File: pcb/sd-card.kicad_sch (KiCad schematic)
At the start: 7 parts, among them J7 MicroSD_5033981892, U7 AP22615AWU-7

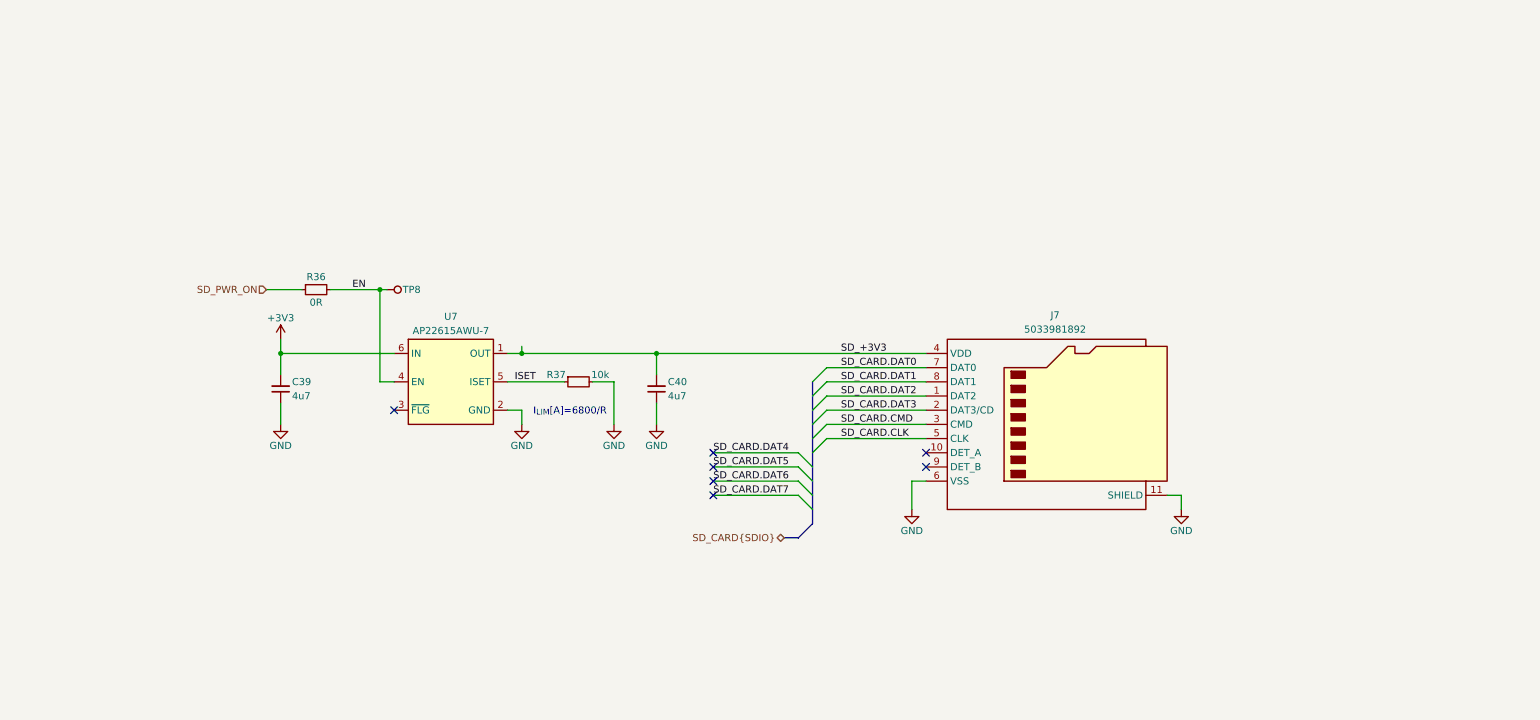
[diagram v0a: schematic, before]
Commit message: [#5] Refactor the schematic
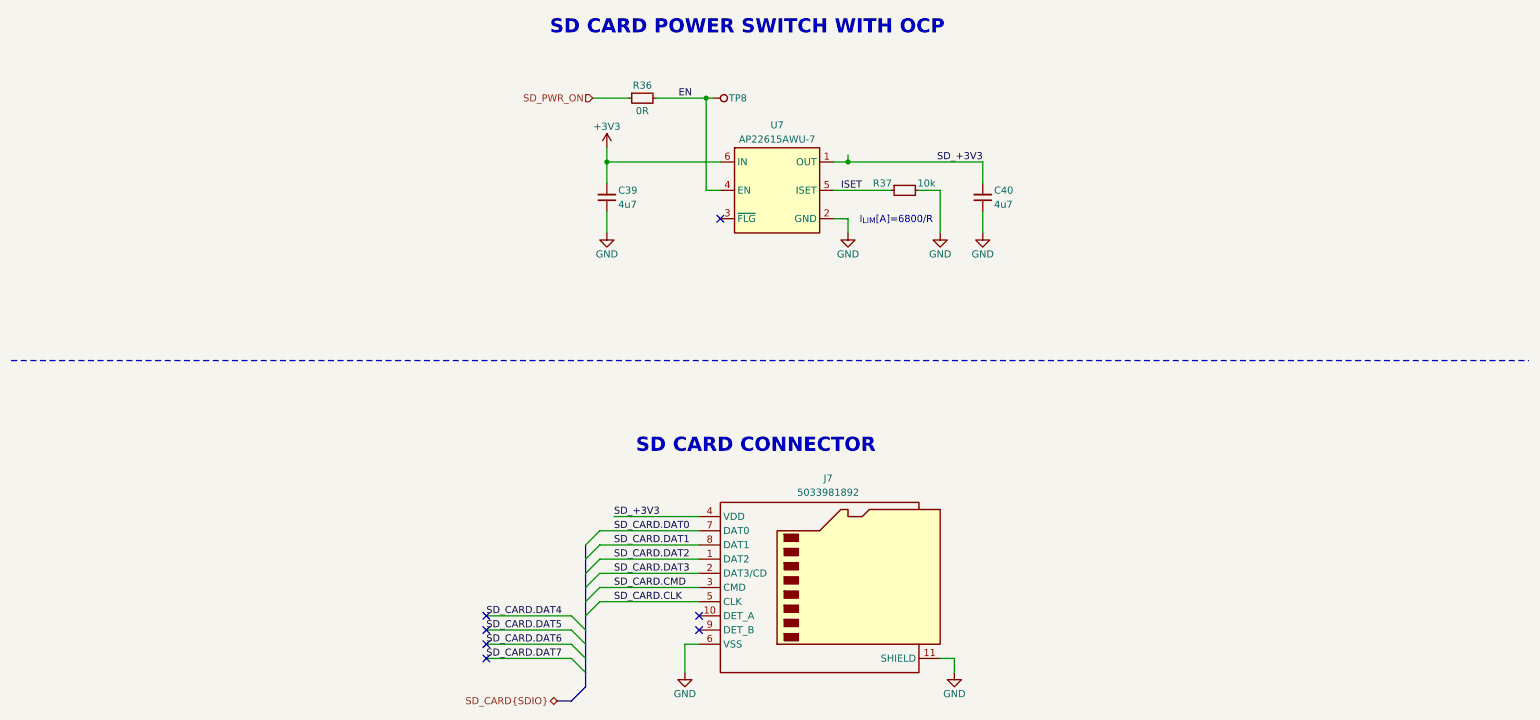
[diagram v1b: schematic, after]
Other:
- note added: "SD CARD CONNECTOR"
- note added: "SD CARD POWER SWITCH WITH OCP"
- moved on the sheet: C39, C40, J7, R36, R37, TP8, U7

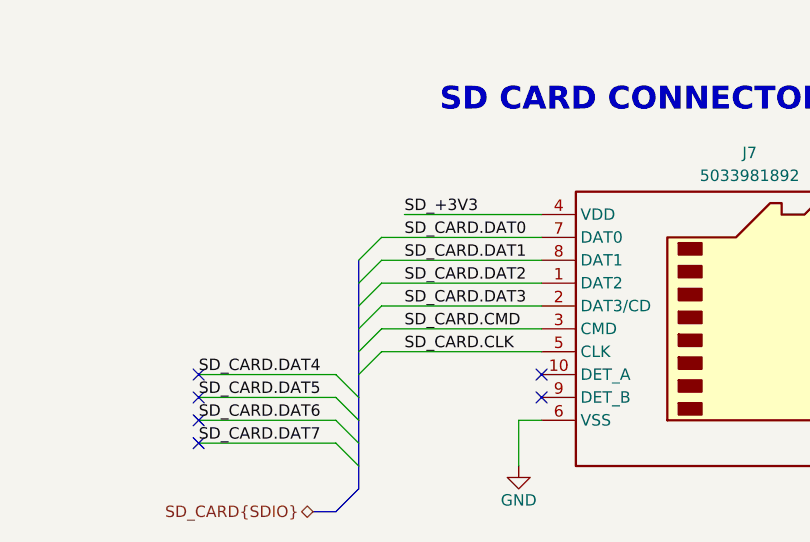
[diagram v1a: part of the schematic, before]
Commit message: [#5] Add decoupling capacitor closer to the SD card, update programming connector from library
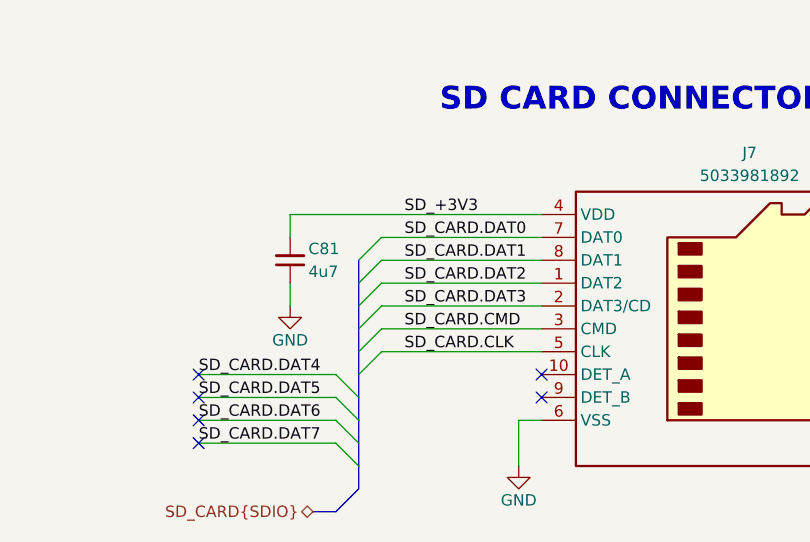
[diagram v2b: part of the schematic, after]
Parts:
- added C81: C-4u7-0402, DW-footprints:C_0402_1005Metric, symbol DW-capacitors:C-4u7-0402
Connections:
- net GND: now also C81.1
- net SD_+3V3: now also C81.2
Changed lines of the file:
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@@
+	(wire
+		(pts
+			(xy 107.95 129.54) (xy 107.95 127)
+		)
+		(stroke
+			(width 0)
+			(type default)
+		)
+	)
 	(wire
 		(pts
@@
 		)
 	)
+	(wire
+		(pts
+			(xy 107.95 127) (xy 135.89 127)
+		)
+		(stroke
+			(width 0)
+			(type default)
+		)
+	)
 	(bus
 		(pts
@@
 		)
 	)
+	(wire
+		(pts
+			(xy 107.95 134.62) (xy 107.95 137.16)
+		)
+		(stroke
+			(width 0)
+			(type default)
+		)
+	)
 	(bus
 		(pts
@@
 		(pts
 			(xy 186.69 72.39) (xy 186.69 76.2)
-		)
-		(stroke
-			(width 0)
-			(type default)
-		)
-	)
-	(wire
-		(pts
-			(xy 120.65 127) (xy 135.89 127)
 		)
 		(stroke
@@
 					(size 1.27 1.27)
 					(italic yes)
+				)
+			)
+		)
+	)
+	(symbol
+		(lib_id "DW-capacitors:C-4u7-0402")
+		(at 107.95 134.62 90)
+		(unit 1)
+		(exclude_from_sim no)
+		(in_bom yes)
+		(on_board yes)
+		(dnp no)
+		(property "Reference" "C81"
+			(at 109.982 130.81 90)
+			(effects
+				(font
+					(size 1.27 1.27)
+					(thickness 0.15)
+				)
+				(justify right)
+			)
+		)
+		(property "Value" "C-4u7-0402"
+			(at 110.49 121.92 0)
+			(effects
+				(font
+					(size 1.27 1.27)
+					(thickness 0.15)
+				)
+				(justify left bottom)
+				(hide yes)
+			)
+		)
+		(property "Footprint" "DW-footprints:C_0402_1005Metric"
+			(at 113.03 121.92 0)
+			(effects
+				(font
+					(size 1.27 1.27)
+					(thickness 0.15)
+				)
+				(justify left bottom)
+				(hide yes)
+			)
+		)
+		(property "Datasheet" "https://lcsc.com/datasheet/lcsc_datasheet_2304140030_Samsung-Electro-Mechanics-CL05A475MP5NRNC_C23733.pdf"
+			(at 115.57 121.92 0)
+			(effects
+				(font
+					(size 1.27 1.27)
+					(thickness 0.15)
+				)
+				(justify left bottom)
+				(hide yes)
+			)
+		)
+		(property "Description" "10V 4.7uF X5R ±20% 0402 Multilayer Ceramic Capacitors MLCC - SMD/SMT ROHS"
+			(at 118.11 121.92 0)
+			(effects
+				(font
+					(size 1.27 1.27)
+					(thickness 0.15)
+				)
+				(justify left bottom)
+				(hide yes)
+			)
+		)
+		(property "Manufacturer" "Samsung Electro-Mechanics"
+			(at 120.65 121.92 0)
+			(effects
+				(font
+					(size 1.27 1.27)
+					(thickness 0.15)
+				)
+				(justify left bottom)
+				(hide yes)
+			)
+		)
+		(property "MPN" "CL05A475MP5NRNC"
+			(at 123.19 121.92 0)
+			(effects
+				(font
+					(size 1.27 1.27)
+					(thickness 0.15)
+				)
+				(justify left bottom)
+				(hide yes)
+			)
+		)
+		(property "LCSC" "C23733"
+			(at 125.73 121.92 0)
+			(effects
+				(font
+					(size 1.27 1.27)
+					(thickness 0.15)
+				)
+				(justify left bottom)
+				(hide yes)
+			)
+		)
+		(property "Val" "4u7"
+			(at 109.982 133.35 90)
+			(effects
+				(font
+					(size 1.27 1.27)
+					(thickness 0.15)
+				)
+				(justify right)
+			)
+		)
+		(property "Tolerance" "20%"
+			(at 130.81 121.92 0)
+			(effects
+				(font
+					(size 1.27 1.27)
+					(thickness 0.15)
+				)
+				(justify left bottom)
+				(hide yes)
+			)
+		)
+		(property "Voltage" "10V"
+			(at 133.35 121.92 0)
+			(effects
+				(font
+					(size 1.27 1.27)
+					(thickness 0.15)
+				)
+				(justify left bottom)
+				(hide yes)
+			)
+		)
+		(property "Dielectric" "X5R"
+			(at 135.89 121.92 0)
+			(effects
+				(font
+					(size 1.27 1.27)
+					(thickness 0.15)
+				)
+				(justify left bottom)
+				(hide yes)
+			)
+		)
+		(pin "1"
+		)
+		(pin "2"
+		)
+		(instances
+			(project "cm5-module"
+				(path "/090a8e41-87a8-4fb1-998b-60a2c0dc4cee/df5d742e-fec8-4307-bd86-008404d5e8ea"
+					(reference "C81")
+					(unit 1)
 				)
 			)
@@
 					(unit 1)
 				)
+			)
+		)
+	)
+	(symbol
+		(lib_id "DW-power-symbols:GND")
+		(at 107.95 137.16 0)
+		(unit 1)
+		(exclude_from_sim no)
+		(in_bom yes)
+		(on_board yes)
+		(dnp no)
+		(property "Reference" "#PWR0213"
+			(at 107.95 143.51 0)
+			(effects
+				(font
+					(size 1.27 1.27)
+				)
+				(hide yes)
+			)
+		)
+		(property "Value" "GND"
+			(at 107.95 140.97 0)
+			(effects
+				(font
+					(size 1.27 1.27)
+				)
+			)
+		)
+		(property "Footprint" ""
+			(at 107.95 137.16 0)
+			(effects
+				(font
+					(size 1.27 1.27)
+				)
+				(hide yes)
+			)
+		)
+		(property "Datasheet" ""
+			(at 107.95 137.16 0)
+			(effects
+				(font
+					(size 1.27 1.27)
+				)
+				(hide yes)
+			)
+		)
+		(property "Description" "Power symbol creates a global label with name \"GND\" , ground"
+			(at 107.95 137.16 0)
+			(effects
+				(font
+					(size 1.27 1.27)
+				)
+				(hide yes)
+			)
+		)
+		(pin "1"
+		)
+		(instances
+			(project "cm5-module"
+				(path "/090a8e41-87a8-4fb1-998b-60a2c0dc4cee/df5d742e-fec8-4307-bd86-008404d5e8ea"
+					(reference "#PWR0213")
+					(unit 1)
+				)
